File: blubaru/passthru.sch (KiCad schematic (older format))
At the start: 0 parts

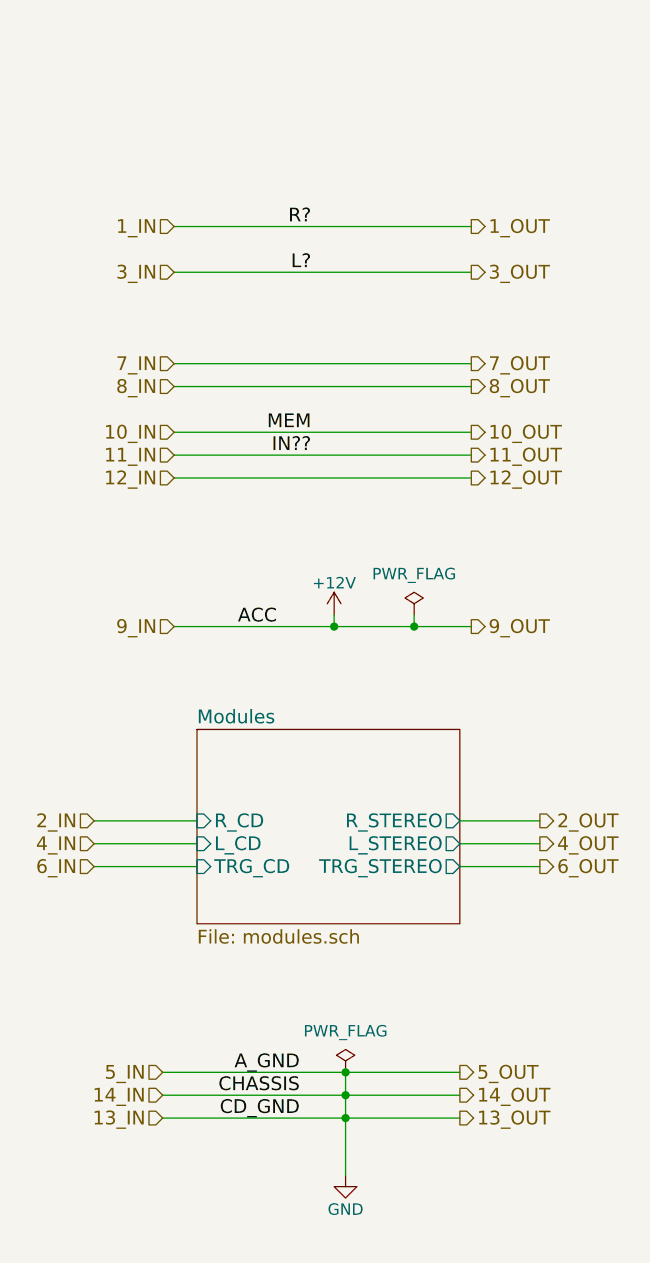
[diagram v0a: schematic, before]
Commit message: Create footprints for breakout boards
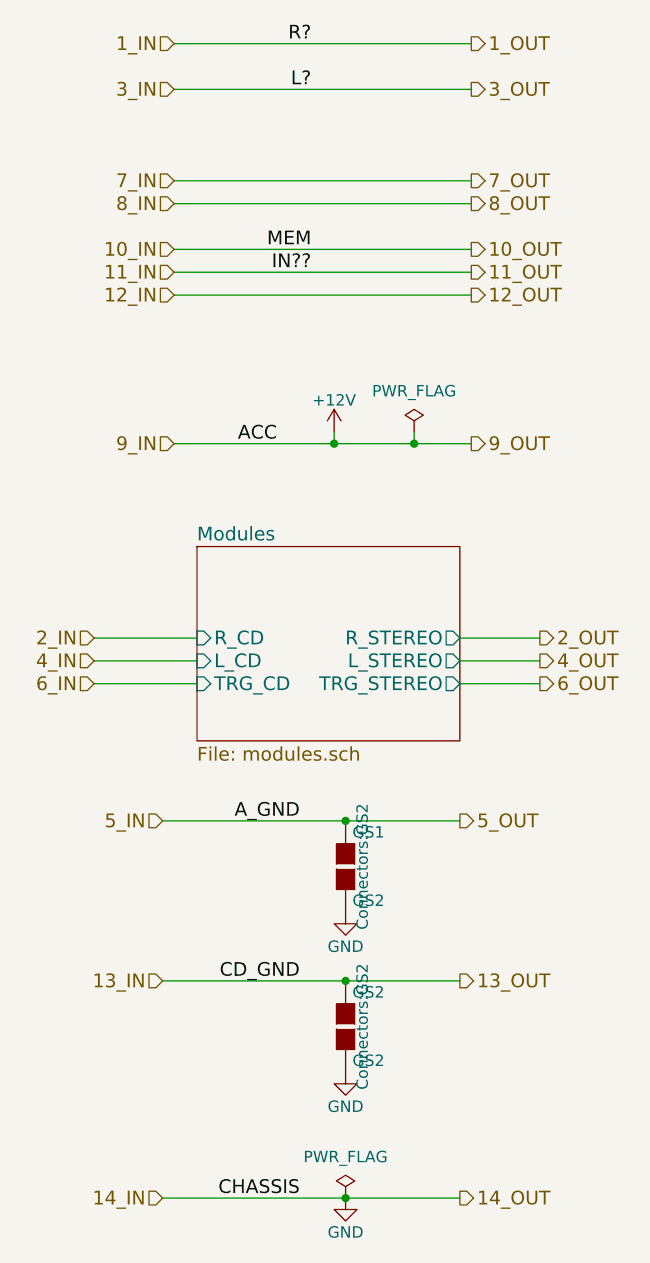
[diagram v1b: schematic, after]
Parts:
- added GS1, GS2: GS2, Connectors:GS2, symbol GS2
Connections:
- net GND: now also GS1.2 (G2), GS2.2 (G2)
- new net 13_IN: GS2.1 (G1)
- new net 5_IN: GS1.1 (G1)
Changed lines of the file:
@@
 encoding utf-8
 Sheet 2 8
-Title ""
-Date ""
+Title "Blubaru"
+Date "2017-02-28"
 Rev ""
 Comp ""
@@
 $EndDescr
 Wire Wire Line
-	4700 2000 6000 2000
+	4700 1200 6000 1200
+Wire Wire Line
+	4700 1400 6000 1400
+Wire Wire Line
+	4650 4600 5950 4600
+Wire Wire Line
+	4700 1800 6000 1800
+Wire Wire Line
+	4700 1900 6000 1900
+Wire Wire Line
+	4700 2950 6000 2950
+Wire Wire Line
+	4700 2100 6000 2100
 Wire Wire Line
 	4700 2200 6000 2200
 Wire Wire Line
-	4650 5700 5950 5700
-Wire Wire Line
-	4700 2600 6000 2600
-Wire Wire Line
-	4700 2700 6000 2700
-Wire Wire Line
-	4700 3750 6000 3750
-Wire Wire Line
-	4700 2900 6000 2900
-Wire Wire Line
-	4700 3000 6000 3000
-Wire Wire Line
-	4700 3100 6000 3100
-Wire Wire Line
-	4650 5900 5950 5900
-Wire Wire Line
-	4650 5800 5950 5800
-Text HLabel 4700 2000 0    60   Input ~ 0
+	4700 2300 6000 2300
+Wire Wire Line
+	4650 5300 5950 5300
+Wire Wire Line
+	4650 6250 5950 6250
+Text HLabel 4700 1200 0    60   Input ~ 0
 1_IN
-Text HLabel 4350 4600 0    60   Input ~ 0
+Text HLabel 4350 3800 0    60   Input ~ 0
 2_IN
+Text HLabel 4700 1400 0    60   Input ~ 0
+3_IN
+Text HLabel 4350 3900 0    60   Input ~ 0
+4_IN
+Text HLabel 4650 4600 0    60   Input ~ 0
+5_IN
+Text HLabel 4350 4000 0    60   Input ~ 0
+6_IN
+Text HLabel 4700 1800 0    60   Input ~ 0
+7_IN
+Text HLabel 4700 1900 0    60   Input ~ 0
+8_IN
+Text HLabel 4700 2950 0    60   Input ~ 0
+9_IN
+Text HLabel 4700 2100 0    60   Input ~ 0
+10_IN
 Text HLabel 4700 2200 0    60   Input ~ 0
-3_IN
-Text HLabel 4350 4700 0    60   Input ~ 0
-4_IN
-Text HLabel 4650 5700 0    60   Input ~ 0
-5_IN
-Text HLabel 4350 4800 0    60   Input ~ 0
-6_IN
-Text HLabel 4700 2600 0    60   Input ~ 0
-7_IN
-Text HLabel 4700 2700 0    60   Input ~ 0
-8_IN
-Text HLabel 4700 3750 0    60   Input ~ 0
-9_IN
-Text HLabel 4700 2900 0    60   Input ~ 0
-10_IN
-Text HLabel 4700 3000 0    60   Input ~ 0
 11_IN
-Text HLabel 4700 3100 0    60   Input ~ 0
+Text HLabel 4700 2300 0    60   Input ~ 0
 12_IN
-Text HLabel 4650 5900 0    60   Input ~ 0
+Text HLabel 4650 5300 0    60   Input ~ 0
 13_IN
-Text HLabel 4650 5800 0    60   Input ~ 0
+Text HLabel 4650 6250 0    60   Input ~ 0
 14_IN
-Text HLabel 6000 2000 2    60   Output ~ 0
+Text HLabel 6000 1200 2    60   Output ~ 0
 1_OUT
-Text HLabel 6300 4600 2    60   Output ~ 0
+Text HLabel 6300 3800 2    60   Output ~ 0
 2_OUT
+Text HLabel 6000 1400 2    60   Output ~ 0
+3_OUT
+Text HLabel 6300 3900 2    60   Output ~ 0
+4_OUT
+Text HLabel 5950 4600 2    60   Output ~ 0
+5_OUT
+Text HLabel 6300 4000 2    60   Output ~ 0
+6_OUT
+Text HLabel 6000 1800 2    60   Output ~ 0
+7_OUT
+Text HLabel 6000 1900 2    60   Output ~ 0
+8_OUT
+Text HLabel 6000 2950 2    60   Output ~ 0
+9_OUT
+Text HLabel 6000 2100 2    60   Output ~ 0
+10_OUT
 Text HLabel 6000 2200 2    60   Output ~ 0
-3_OUT
-Text HLabel 6300 4700 2    60   Output ~ 0
-4_OUT
-Text HLabel 5950 5700 2    60   Output ~ 0
-5_OUT
-Text HLabel 6300 4800 2    60   Output ~ 0
-6_OUT
-Text HLabel 6000 2600 2    60   Output ~ 0
-7_OUT
-Text HLabel 6000 2700 2    60   Output ~ 0
-8_OUT
-Text HLabel 6000 3750 2    60   Output ~ 0
-9_OUT
-Text HLabel 6000 2900 2    60   Output ~ 0
-10_OUT
-Text HLabel 6000 3000 2    60   Output ~ 0
 11_OUT
-Text HLabel 6000 3100 2    60   Output ~ 0
+Text HLabel 6000 2300 2    60   Output ~ 0
 12_OUT
-Text HLabel 5950 5900 2    60   Output ~ 0
+Text HLabel 5950 5300 2    60   Output ~ 0
 13_OUT
-Text HLabel 5950 5800 2    60   Output ~ 0
+Text HLabel 5950 6250 2    60   Output ~ 0
 14_OUT
-Text Label 5300 2000 2    60   ~ 0
+Text Label 5300 1200 2    60   ~ 0
 R?
+Text Label 5300 1400 2    60   ~ 0
+L?
+Text Label 5250 4600 2    60   ~ 0
+A_GND
+Text Label 5150 2950 2    60   ~ 0
+ACC
+Text Label 5300 2100 2    60   ~ 0
+MEM
 Text Label 5300 2200 2    60   ~ 0
-L?
-Text Label 5250 5700 2    60   ~ 0
-A_GND
-Text Label 5150 3750 2    60   ~ 0
-ACC
-Text Label 5300 2900 2    60   ~ 0
-MEM
-Text Label 5300 3000 2    60   ~ 0
 IN??
-Text Label 5250 5900 2    60   ~ 0
+Text Label 5250 5300 2    60   ~ 0
 CD_GND
-Text Label 5250 5800 2    60   ~ 0
+Text Label 5250 6250 2    60   ~ 0
 CHASSIS
 Wire Wire Line
-	4350 4600 4800 4600
-Wire Wire Line
-	4350 4700 4800 4700
-Wire Wire Line
-	4350 4800 4800 4800
-Wire Wire Line
-	5950 4600 6300 4600
-Wire Wire Line
-	5950 4700 6300 4700
-Wire Wire Line
-	5950 4800 6300 4800
+	4350 3800 4800 3800
+Wire Wire Line
+	4350 3900 4800 3900
+Wire Wire Line
+	4350 4000 4800 4000
+Wire Wire Line
+	5950 3800 6300 3800
+Wire Wire Line
+	5950 3900 6300 3900
+Wire Wire Line
+	5950 4000 6300 4000
 $Sheet
-S 4800 4200 1150 850
+S 4800 3400 1150 850
 U 58B1273D
 F0 "Modules" 60
 F1 "modules.sch" 60
-F2 "L_CD" I L 4800 4700 60
-F3 "R_CD" I L 4800 4600 60
-F4 "L_STEREO" O R 5950 4700 60
-F5 "R_STEREO" O R 5950 4600 60
-F6 "TRG_STEREO" O R 5950 4800 60
-F7 "TRG_CD" I L 4800 4800 60
+F2 "L_CD" I L 4800 3900 60
+F3 "R_CD" I L 4800 3800 60
+F4 "L_STEREO" O R 5950 3900 60
+F5 "R_STEREO" O R 5950 3800 60
+F6 "TRG_STEREO" O R 5950 4000 60
+F7 "TRG_CD" I L 4800 4000 60
 $EndSheet
 $Comp
 L GND #PWR01
 U 1 1 58B1285E
-P 5450 6150
-F 0 "#PWR01" H 5450 5900 50  0001 C CNN
-F 1 "GND" H 5450 6000 50  0000 C CNN
-F 2 "" H 5450 6150 50  0000 C CNN
-F 3 "" H 5450 6150 50  0000 C CNN
-	1    5450 6150
-	1    0    0    -1
-$EndComp
-Wire Wire Line
-	5450 5700 5450 6150
-Connection ~ 5450 5900
-Connection ~ 5450 5800
-Connection ~ 5450 5700
+P 5450 6250
+F 0 "#PWR01" H 5450 6000 50  0001 C CNN
+F 1 "GND" H 5450 6100 50  0000 C CNN
+F 2 "" H 5450 6250 50  0000 C CNN
+F 3 "" H 5450 6250 50  0000 C CNN
+	1    5450 6250
+	1    0    0    -1
+$EndComp
+Connection ~ 5450 5300
+Connection ~ 5450 6250
+Connection ~ 5450 4600
 $Comp
 L PWR_FLAG #FLG02
 U 1 1 58B12AA7
-P 5750 3700
-F 0 "#FLG02" H 5750 3795 50  0001 C CNN
-F 1 "PWR_FLAG" H 5750 3880 50  0000 C CNN
-F 2 "" H 5750 3700 50  0000 C CNN
-F 3 "" H 5750 3700 50  0000 C CNN
-	1    5750 3700
-	1    0    0    -1
-$EndComp
-$Comp
-L PWR_FLAG #FLG03
+P 5750 2900
+F 0 "#FLG02" H 5750 2995 50  0001 C CNN
+F 1 "PWR_FLAG" H 5750 3080 50  0000 C CNN
+F 2 "" H 5750 2900 50  0000 C CNN
+F 3 "" H 5750 2900 50  0000 C CNN
+	1    5750 2900
+	1    0    0    -1
+$EndComp
+$Comp
+L +12V #PWR03
+U 1 1 58B12C1E
+P 5400 2900
+F 0 "#PWR03" H 5400 2750 50  0001 C CNN
+F 1 "+12V" H 5400 3040 50  0000 C CNN
+F 2 "" H 5400 2900 50  0000 C CNN
+F 3 "" H 5400 2900 50  0000 C CNN
+	1    5400 2900
+	1    0    0    -1
+$EndComp
+Wire Wire Line
+	5750 2900 5750 2950
+Connection ~ 5750 2950
+Wire Wire Line
+	5400 2900 5400 2950
+Connection ~ 5400 2950
+$Comp
+L GS2 GS1
+U 1 1 58B4F2F1
+P 5450 4800
+F 0 "GS1" H 5550 4950 50  0000 C CNN
+F 1 "GS2" H 5550 4651 50  0000 C CNN
+F 2 "Connectors:GS2" V 5524 4800 50  0000 C CNN
+F 3 "" H 5450 4800 50  0000 C CNN
+	1    5450 4800
+	1    0    0    -1
+$EndComp
+$Comp
+L PWR_FLAG #FLG04
 U 1 1 58B12B41
+P 5450 6250
+F 0 "#FLG04" H 5450 6345 50  0001 C CNN
+F 1 "PWR_FLAG" H 5450 6430 50  0000 C CNN
+F 2 "" H 5450 6250 50  0000 C CNN
+F 3 "" H 5450 6250 50  0000 C CNN
+	1    5450 6250
+	1    0    0    -1
+$EndComp
+$Comp
+L GND #PWR05
+U 1 1 58B4FAC7
+P 5450 5000
+F 0 "#PWR05" H 5450 4750 50  0001 C CNN
+F 1 "GND" H 5450 4850 50  0000 C CNN
+F 2 "" H 5450 5000 50  0000 C CNN
+F 3 "" H 5450 5000 50  0000 C CNN
+	1    5450 5000
+	1    0    0    -1
+$EndComp
+$Comp
+L GS2 GS2
+U 1 1 58B4FB59
+P 5450 5500
+F 0 "GS2" H 5550 5650 50  0000 C CNN
+F 1 "GS2" H 5550 5351 50  0000 C CNN
+F 2 "Connectors:GS2" V 5524 5500 50  0000 C CNN
+F 3 "" H 5450 5500 50  0000 C CNN
+	1    5450 5500
+	1    0    0    -1
+$EndComp
+$Comp
+L GND #PWR06
+U 1 1 58B4FBCF
 P 5450 5700
-F 0 "#FLG03" H 5450 5795 50  0001 C CNN
-F 1 "PWR_FLAG" H 5450 5880 50  0000 C CNN
+F 0 "#PWR06" H 5450 5450 50  0001 C CNN
+F 1 "GND" H 5450 5550 50  0000 C CNN
 F 2 "" H 5450 5700 50  0000 C CNN
 F 3 "" H 5450 5700 50  0000 C CNN
@@
 	1    0    0    -1
 $EndComp
-$Comp
-L +12V #PWR04
-U 1 1 58B12C1E
-P 5400 3700
-F 0 "#PWR04" H 5400 3550 50  0001 C CNN
-F 1 "+12V" H 5400 3840 50  0000 C CNN
-F 2 "" H 5400 3700 50  0000 C CNN
-F 3 "" H 5400 3700 50  0000 C CNN
-	1    5400 3700
-	1    0    0    -1
-$EndComp
-Wire Wire Line
-	5750 3700 5750 3750
-Connection ~ 5750 3750
-Wire Wire Line
-	5400 3700 5400 3750
-Connection ~ 5400 3750
 $EndSCHEMATC
